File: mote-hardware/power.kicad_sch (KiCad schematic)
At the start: 5 parts, among them J1 USB_B_Micro, U2 NCP1117-3.3_SOT223, U6 HUSB238A-xxxxx-QN16R

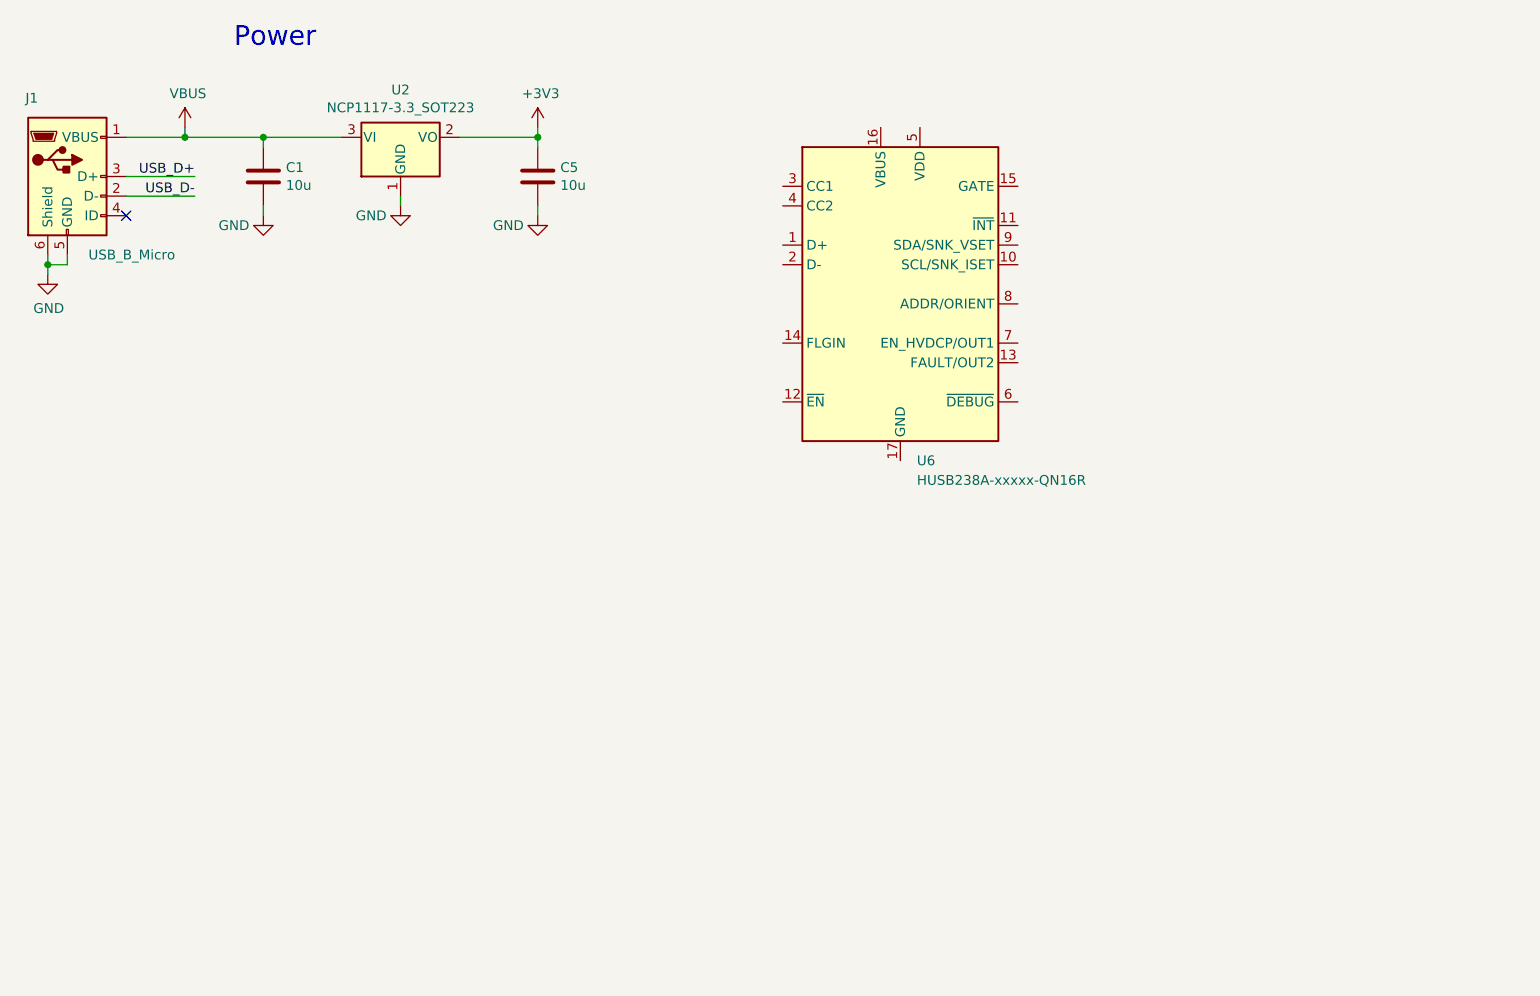
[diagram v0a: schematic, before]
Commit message: Implement motor, power, imu, status LED schematics
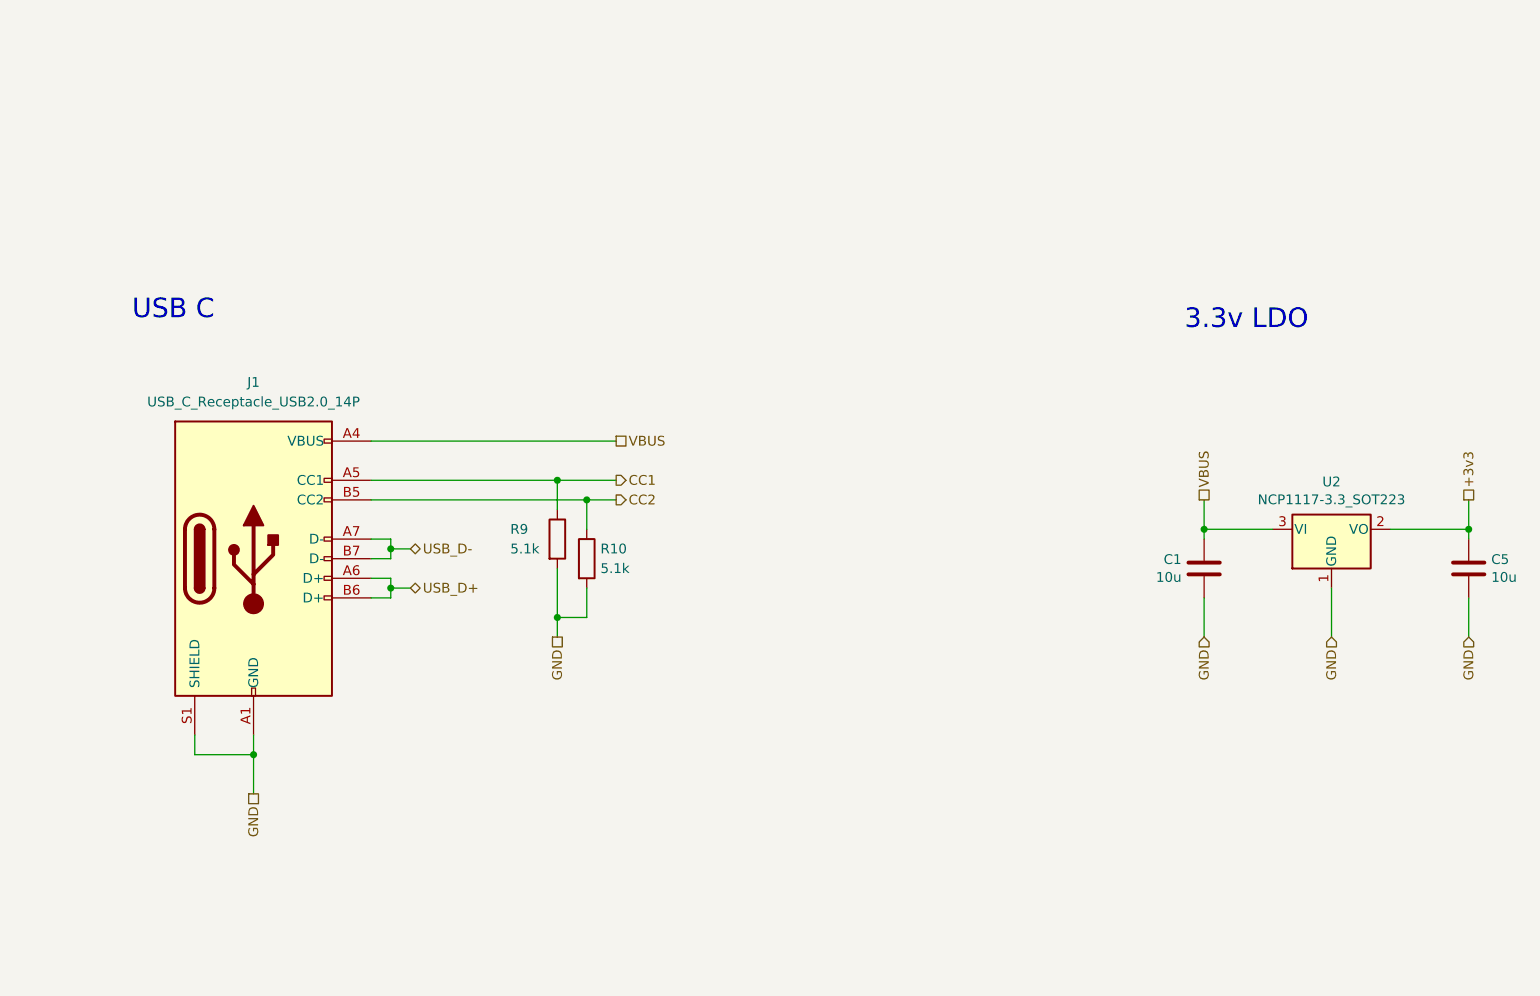
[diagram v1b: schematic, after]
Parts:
- removed J1: USB_B_Micro, Connector_USB:USB_Micro-B_Amphenol_10103594-0001LF_Horizontal, symbol Connector:USB_B_Micro
- removed U6: HUSB238A-xxxxx-QN16R, Package_DFN_QFN:WQFN-16-1EP_3x3mm_P0.5mm_EP1.75x1.75mm, symbol Interface_USB:HUSB238A-xxxxx-QN16R
- added J1: USB_C_Receptacle_USB2.0_14P, symbol Connector:USB_C_Receptacle_USB2.0_14P
- added R10, R9: 5.1k, symbol Device:R
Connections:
- net GND: now also J1.A1 (GND), J1.A12 (GND), J1.B1 (GND), J1.B12 (GND), J1.S1 (SHIELD), R10.2, R9.2
- net USB_D+: now also J1.A6 (D+), J1.B6 (D+)
- net USB_D-: now also J1.A7 (D-), J1.B7 (D-)
- net VBUS: now also J1.A4 (VBUS), J1.A9 (VBUS), J1.B4 (VBUS), J1.B9 (VBUS)
- net +3V3 renamed +3v3
- new net CC1: J1.A5 (CC1), R9.1
- new net CC2: J1.B5 (CC2), R10.1
- no-connect marks 1 -> 0
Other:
- note added: "3.3v LDO"
- note added: "USB C"
- note removed: "Power"
- moved on the sheet: C1, C5, U2

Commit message: First draft schematic complete
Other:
- company: (none) -> github.com/usedhondacivic/mote
- title: (none) -> Mote
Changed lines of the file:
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@@
 	(generator_version "9.0")
 	(paper "A4")
+	(title_block
+		(title "Mote")
+		(date "2025-12-30")
+		(rev "V0.0.0")
+		(company "github.com/usedhondacivic/mote")
+	)
 	(text "USB C"
 		(exclude_from_sim no)

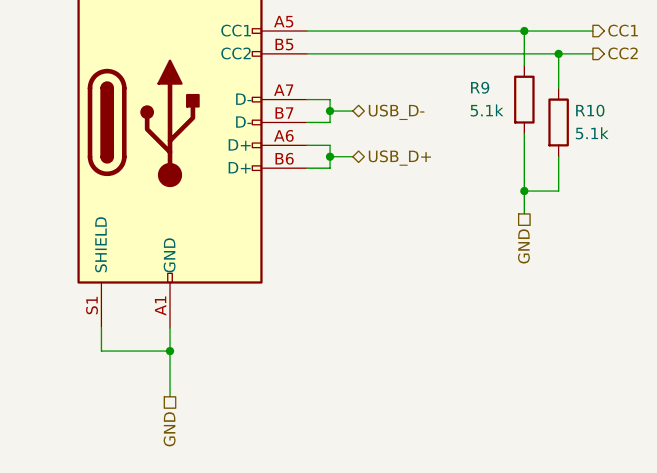
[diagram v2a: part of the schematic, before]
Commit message: Footprint assignments
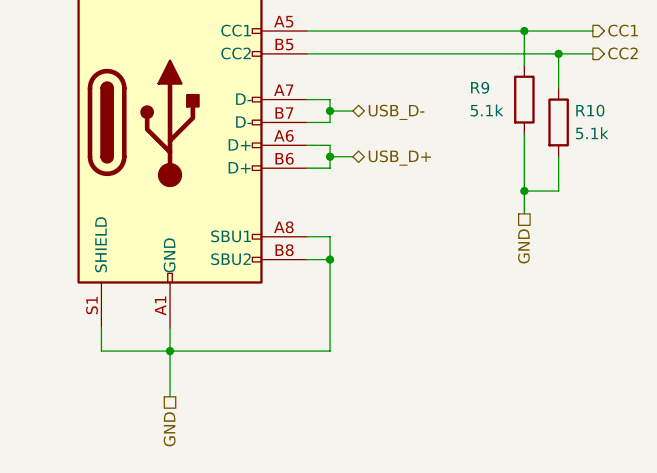
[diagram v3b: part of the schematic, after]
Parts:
- J1: footprint (none) -> Connector_USB:USB_C_Receptacle_G-Switch_GT-USB-7010ASV; symbol Connector:USB_C_Receptacle_USB2.0_14P -> Connector:USB_C_Receptacle_USB2.0_16P
- R10, R9: footprint (none) -> Resistor_SMD:R_0402_1005Metric
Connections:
- net GND: now also J1.A8 (SBU1), J1.B8 (SBU2)
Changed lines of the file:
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@@
+	)
+	(junction
+		(at 83.82 114.3)
+		(diameter 0)
+		(color 0 0 0 0)
 	)
 	(junction
@@
 	(wire
 		(pts
+			(xy 83.82 124.46) (xy 66.04 124.46)
+		)
+		(stroke
+			(width 0)
+			(type default)
+		)
+	)
+	(wire
+		(pts
 			(xy 58.42 124.46) (xy 66.04 124.46)
 		)
@@
 	(wire
 		(pts
+			(xy 83.82 111.76) (xy 83.82 114.3)
+		)
+		(stroke
+			(width 0)
+			(type default)
+		)
+	)
+	(wire
+		(pts
 			(xy 105.41 106.68) (xy 109.22 106.68)
 		)
@@
 	(wire
 		(pts
+			(xy 81.28 111.76) (xy 83.82 111.76)
+		)
+		(stroke
+			(width 0)
+			(type default)
+		)
+	)
+	(wire
+		(pts
 			(xy 81.28 83.82) (xy 113.03 83.82)
 		)
@@
 	(wire
 		(pts
+			(xy 81.28 114.3) (xy 83.82 114.3)
+		)
+		(stroke
+			(width 0)
+			(type default)
+		)
+	)
+	(wire
+		(pts
 			(xy 189.23 95.25) (xy 189.23 96.52)
 		)
@@
 		(pts
 			(xy 83.82 97.79) (xy 83.82 96.52)
+		)
+		(stroke
+			(width 0)
+			(type default)
+		)
+	)
+	(wire
+		(pts
+			(xy 83.82 114.3) (xy 83.82 124.46)
 		)
 		(stroke
@@
 	)
 	(symbol
-		(lib_id "Connector:USB_C_Receptacle_USB2.0_14P")
+		(lib_id "Connector:USB_C_Receptacle_USB2.0_16P")
 		(at 66.04 99.06 0)
 		(unit 1)
@@
 			)
 		)
-		(property "Footprint" ""
+		(property "Footprint" "Connector_USB:USB_C_Receptacle_G-Switch_GT-USB-7010ASV"
 			(at 69.85 99.06 0)
 			(effects
@@
 			)
 		)
-		(property "Description" "USB 2.0-only 14P Type-C Receptacle connector"
+		(property "Description" "USB 2.0-only 16P Type-C Receptacle connector"
 			(at 66.04 99.06 0)
 			(effects
@@
 		)
 		(pin "A12"
+		)
+		(pin "A8"
+		)
+		(pin "B8"
 		)
 		(instances
@@
 			)
 		)
-		(property "Footprint" ""
+		(property "Footprint" "Resistor_SMD:R_0402_1005Metric"
 			(at 107.442 99.06 90)
 			(effects
@@
 			)
 		)
-		(property "Footprint" ""
+		(property "Footprint" "Resistor_SMD:R_0402_1005Metric"
 			(at 103.632 96.52 90)
 			(effects

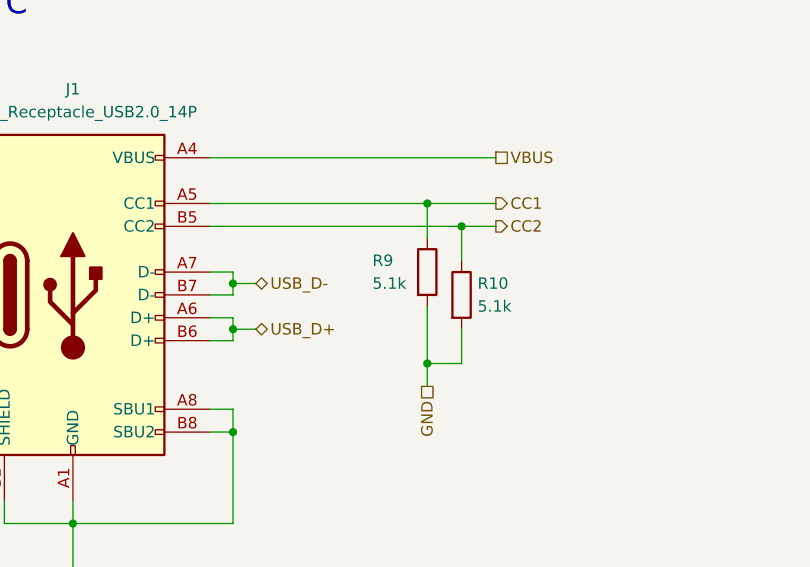
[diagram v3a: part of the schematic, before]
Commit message: Get pcb ready for first prototype order (#31)
Co-authored-by: Kyle Mui <44453997+KyleMui@users.noreply.github.com>
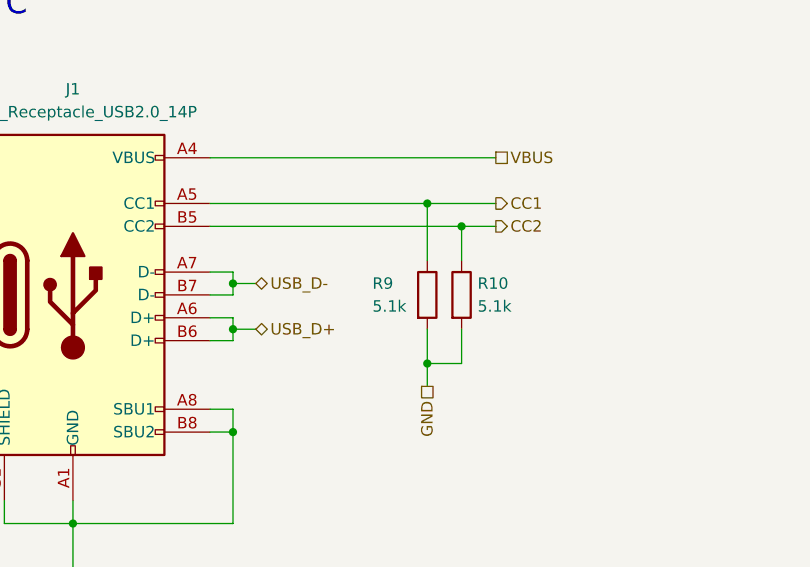
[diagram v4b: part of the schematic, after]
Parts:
- C1, C5: footprint Capacitor_SMD:C_0805_2012Metric -> PCM_JLCPCB:C_0805
- R10, R9: footprint Resistor_SMD:R_0402_1005Metric -> PCM_JLCPCB:R_0402
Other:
- company: github.com/usedhondacivic/mote -> github.com/empriselab/mote-core
- moved on the sheet: R9
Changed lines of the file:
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@@
 	(title_block
 		(title "Mote")
-		(date "2025-12-30")
+		(date "2026-03-31")
 		(rev "V0.0.0")
-		(company "github.com/usedhondacivic/mote")
+		(company "github.com/empriselab/mote-core")
 	)
 	(text "USB C"
@@
 	(wire
 		(pts
-			(xy 105.41 100.33) (xy 105.41 106.68)
+			(xy 105.41 102.87) (xy 105.41 106.68)
 		)
 		(stroke
@@
 	(wire
 		(pts
-			(xy 105.41 88.9) (xy 105.41 92.71)
+			(xy 105.41 88.9) (xy 105.41 95.25)
 		)
 		(stroke
@@
 			)
 		)
-		(property "Footprint" "Capacitor_SMD:C_0805_2012Metric"
+		(property "Footprint" "PCM_JLCPCB:C_0805"
 			(at 188.2648 104.14 0)
 			(effects
@@
 			)
 		)
-		(property "Footprint" "Capacitor_SMD:C_0805_2012Metric"
+		(property "Footprint" "PCM_JLCPCB:C_0805"
 			(at 224.4852 104.14 0)
 			(effects
@@
 		)
 		(instances
-			(project ""
+			(project "mote-hardware"
 				(path "/94683f5c-9cd9-448e-be96-9792537b5cb8/b87252c5-15f5-4304-a4f0-d9bd6e688e51"
 					(reference "J1")
@@
 			)
 		)
-		(property "Footprint" "Resistor_SMD:R_0402_1005Metric"
+		(property "Footprint" "PCM_JLCPCB:R_0402"
 			(at 107.442 99.06 90)
 			(effects
@@
 	(symbol
 		(lib_id "Device:R")
-		(at 105.41 96.52 0)
+		(at 105.41 99.06 0)
 		(unit 1)
 		(exclude_from_sim no)
@@
 		(dnp no)
 		(property "Reference" "R9"
-			(at 99.314 95.25 0)
+			(at 99.314 97.79 0)
 			(effects
 				(font
@@
 		)
 		(property "Value" "5.1k"
-			(at 99.314 97.79 0)
+			(at 99.314 100.33 0)
 			(effects
 				(font
@@
 			)
 		)
-		(property "Footprint" "Resistor_SMD:R_0402_1005Metric"
-			(at 103.632 96.52 90)
+		(property "Footprint" "PCM_JLCPCB:R_0402"
+			(at 103.632 99.06 90)
 			(effects
 				(font
@@
 		)
 		(property "Datasheet" "~"
-			(at 105.41 96.52 0)
+			(at 105.41 99.06 0)
 			(effects
 				(font
@@
 		)
 		(property "Description" "Resistor"
-			(at 105.41 96.52 0)
+			(at 105.41 99.06 0)
 			(effects
 				(font
@@
 		)
 		(instances
-			(project ""
+			(project "mote-hardware"
 				(path "/94683f5c-9cd9-448e-be96-9792537b5cb8/b87252c5-15f5-4304-a4f0-d9bd6e688e51"
 					(reference "R9")

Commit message: Assign LCSC part numbers
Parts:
- C1, C5: LCSC (none) -> C440198
- J1: LCSC (none) -> C2927038
- R10, R9: LCSC (none) -> C25905
- U2: LCSC (none) -> C26537
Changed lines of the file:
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@@
+			)
+		)
+		(property "LCSC" "C26537"
+			(at 205.74 95.25 0)
+			(effects
+				(font
+					(size 1.27 1.27)
+				)
+				(hide yes)
 			)
 		)
@@
 			)
 		)
+		(property "LCSC" "C440198"
+			(at 189.23 100.33 0)
+			(effects
+				(font
+					(size 1.27 1.27)
+				)
+				(hide yes)
+			)
+		)
 		(pin "1"
 		)
@@
 					(size 1.27 1.27)
 				)
+			)
+		)
+		(property "LCSC" "C440198"
+			(at 223.52 100.33 0)
+			(effects
+				(font
+					(size 1.27 1.27)
+				)
+				(hide yes)
 			)
 		)
@@
 			)
 		)
+		(property "LCSC" "C2927038"
+			(at 66.04 99.06 0)
+			(effects
+				(font
+					(size 1.27 1.27)
+				)
+				(hide yes)
+			)
+		)
 		(pin "S1"
 		)
@@
 			)
 		)
+		(property "LCSC" "C25905"
+			(at 109.22 99.06 0)
+			(effects
+				(font
+					(size 1.27 1.27)
+				)
+				(hide yes)
+			)
+		)
 		(pin "2"
 		)
@@
 			(at 105.41 99.06 0)
 			(effects
+				(font
+					(size 1.27 1.27)
+				)
+				(hide yes)
+			)
+		)
+		(property "LCSC" "C25905"
+			(at 105.41 99.06 0)
+			(effects
